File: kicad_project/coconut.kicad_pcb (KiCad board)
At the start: 2 copper layers, 212.6 x 79.2 mm, 88 parts

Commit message: change the layout
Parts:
- K_32: footprint MX_Only:MXOnly-1U-NoLED -> MX_Only:MXOnly-1.25U-NoLED
- K_34: footprint MX_Only:MXOnly-1.5U-NoLED -> MX_Only:MXOnly-1.25U-NoLED
- moved K_33 4.76 mm to (58.7, 68.2)
- moved REF** 3.57 mm to (69.4, 76.0)
- moved K_34 2.38 mm to (80.1, 68.2)
- moved K_32 2.38 mm to (37.2, 68.2)
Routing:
- net col2: track 207.8 -> 209.8 mm
- net col1: track 228.7 -> 229.6 mm

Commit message: fix mismatch
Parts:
- moved D_32 4.76 mm to (48.1, 68.9)
- moved D_33 4.76 mm to (67.2, 68.9)
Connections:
- U_1 pad 10: col3 -> col2
- U_1 pad 7: col0 -> col3
- U_1 pad 8: col1 -> col0
- U_1 pad 9: col2 -> col1
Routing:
- net col3: track 187.8 -> 197.6 mm
- net col2: track 209.8 -> 206.8 mm
- net col1: track 229.6 -> 226.7 mm
- net col0: track 243.3 -> 240.3 mm
- net Net-(D_32-Pad2): track 7.70 -> 10.1 mm
- net Net-(D_34-Pad2): track 12.5 -> 10.1 mm
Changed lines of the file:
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@@
       (net 14 "row2") (pinfunction "D0") (pintype "bidirectional"))
     (pad "7" thru_hole oval locked (at 15.24 12.7 90) (size 1.6 1.6) (drill 0.8) (layers *.Cu *.Mask)
-      (net 1 "col0") (pinfunction "D4") (pintype "bidirectional"))
+      (net 4 "col3") (pinfunction "D4") (pintype "bidirectional"))
     (pad "8" thru_hole oval locked (at 15.24 10.16 90) (size 1.6 1.6) (drill 0.8) (layers *.Cu *.Mask)
-      (net 2 "col1") (pinfunction "C6") (pintype "bidirectional"))
+      (net 1 "col0") (pinfunction "C6") (pintype "bidirectional"))
     (pad "9" thru_hole oval locked (at 15.24 7.62 90) (size 1.6 1.6) (drill 0.8) (layers *.Cu *.Mask)
-      (net 3 "col2") (pinfunction "D7") (pintype "bidirectional"))
+      (net 2 "col1") (pinfunction "D7") (pintype "bidirectional"))
     (pad "10" thru_hole oval locked (at 15.24 5.08 90) (size 1.6 1.6) (drill 0.8) (layers *.Cu *.Mask)
-      (net 4 "col3") (pinfunction "E6") (pintype "bidirectional"))
+      (net 3 "col2") (pinfunction "E6") (pintype "bidirectional"))
     (pad "11" thru_hole oval locked (at 15.24 2.54 90) (size 1.6 1.6) (drill 0.8) (layers *.Cu *.Mask)
       (net 10 "col9") (pinfunction "B4") (pintype "bidirectional"))
@@
   )
   (footprint "Diode_SMD:D_SOD-123" (layer "B.Cu")
-    (at 43.3625 68.893901 90)
+    (at 48.1265 68.893901 90)
     (descr "SOD-123")
     (tags "SOD-123")
@@
   )
   (footprint "Diode_SMD:D_SOD-123" (layer "B.Cu")
-    (at 62.4125 68.893901 90)
+    (at 67.1765 68.893901 90)
     (descr "SOD-123")
     (tags "SOD-123")
@@
   (segment (start 11.9775 27.535) (end 11.9775 41.8225) (width 0.25) (layer "F.Cu") (net 1))
   (segment (start 7.215 8.485) (end 7.215 22.7725) (width 0.25) (layer "F.Cu") (net 1))
-  (via (at 16.74 52.493901) (size 0.8) (drill 0.4) (layers "F.Cu" "B.Cu") (net 1))
-  (segment (start 184.573901 52.493901) (end 192.635 60.555) (width 0.25) (layer "B.Cu") (net 1))
-  (segment (start 16.74 52.493901) (end 184.573901 52.493901) (width 0.25) (layer "B.Cu") (net 1))
+  (via (at 16.74 53.493901) (size 0.8) (drill 0.4) (layers "F.Cu" "B.Cu") (net 1))
+  (segment (start 183.033901 53.493901) (end 16.74 53.493901) (width 0.25) (layer "B.Cu") (net 1))
+  (segment (start 190.095 60.555) (end 183.033901 53.493901) (width 0.25) (layer "B.Cu") (net 1))
   (segment (start 33.4085 65.635) (end 26.9 59.1265) (width 0.25) (layer "F.Cu") (net 2))
   (segment (start 31.0275 40.8545) (end 26.9 44.982) (width 0.25) (layer "F.Cu") (net 2))
@@
   (segment (start 26.265 22.7725) (end 31.0275 27.535) (width 0.25) (layer "F.Cu") (net 2))
   (segment (start 26.265 8.485) (end 26.265 22.7725) (width 0.25) (layer "F.Cu") (net 2))
-  (via (at 26.9 53.493901) (size 0.8) (drill 0.4) (layers "F.Cu" "B.Cu") (net 2))
-  (segment (start 190.095 60.555) (end 183.033901 53.493901) (width 0.25) (layer "B.Cu") (net 2))
-  (segment (start 183.033901 53.493901) (end 26.9 53.493901) (width 0.25) (layer "B.Cu") (net 2))
+  (via (at 26.9 54.493901) (size 0.8) (drill 0.4) (layers "F.Cu" "B.Cu") (net 2))
+  (segment (start 26.9 54.493901) (end 181.493901 54.493901) (width 0.25) (layer "B.Cu") (net 2))
+  (segment (start 181.493901 54.493901) (end 187.555 60.555) (width 0.25) (layer "B.Cu") (net 2))
   (segment (start 50.0775 41.8225) (end 45.315 46.585) (width 0.25) (layer "F.Cu") (net 3))
   (segment (start 54.8405 65.635) (end 45.315 56.1095) (width 0.25) (layer "F.Cu") (net 3))
@@
   (segment (start 45.315 22.7725) (end 50.0775 27.535) (width 0.25) (layer "F.Cu") (net 3))
   (segment (start 45.315 8.485) (end 45.315 22.7725) (width 0.25) (layer "F.Cu") (net 3))
-  (via (at 45.315 54.493901) (size 0.8) (drill 0.4) (layers "F.Cu" "B.Cu") (net 3))
-  (segment (start 181.493901 54.493901) (end 187.555 60.555) (width 0.25) (layer "B.Cu") (net 3))
-  (segment (start 45.315 54.493901) (end 181.493901 54.493901) (width 0.25) (layer "B.Cu") (net 3))
+  (via (at 45.315 55.493901) (size 0.8) (drill 0.4) (layers "F.Cu" "B.Cu") (net 3))
+  (segment (start 179.953901 55.493901) (end 45.315 55.493901) (width 0.25) (layer "B.Cu") (net 3))
+  (segment (start 179.953901 55.493901) (end 185.015 60.555) (width 0.25) (layer "B.Cu") (net 3))
   (segment (start 69.1275 27.535) (end 69.1275 41.8225) (width 0.25) (layer "F.Cu") (net 4))
+  (segment (start 64.365 46.585) (end 64.365 53.728) (width 0.25) (layer "F.Cu") (net 4))
   (segment (start 64.365 8.485) (end 64.365 22.7725) (width 0.25) (layer "F.Cu") (net 4))
   (segment (start 69.1275 41.8225) (end 64.365 46.585) (width 0.25) (layer "F.Cu") (net 4))
-  (segment (start 64.365 56.11) (end 73.89 65.635) (width 0.25) (layer "F.Cu") (net 4))
-  (segment (start 64.365 46.585) (end 64.365 55.523) (width 0.25) (layer "F.Cu") (net 4))
-  (segment (start 64.365 55.523) (end 64.365 56.11) (width 0.25) (layer "F.Cu") (net 4))
+  (segment (start 76.272 65.635) (end 64.365 53.728) (width 0.25) (layer "F.Cu") (net 4))
   (segment (start 64.365 22.7725) (end 69.1275 27.535) (width 0.25) (layer "F.Cu") (net 4))
-  (via (at 64.365 55.493901) (size 0.8) (drill 0.4) (layers "F.Cu" "B.Cu") (net 4))
-  (segment (start 64.365 55.493901) (end 179.953901 55.493901) (width 0.25) (layer "B.Cu") (net 4))
-  (segment (start 179.953901 55.493901) (end 185.015 60.555) (width 0.25) (layer "B.Cu") (net 4))
-  (segment (start 83.415 46.585) (end 83.415 56.493901) (width 0.25) (layer "F.Cu") (net 5))
+  (via (at 64.365 52.493901) (size 0.8) (drill 0.4) (layers "F.Cu" "B.Cu") (net 4))
+  (segment (start 184.573901 52.493901) (end 192.635 60.555) (width 0.25) (layer "B.Cu") (net 4))
+  (segment (start 64.365 52.493901) (end 184.573901 52.493901) (width 0.25) (layer "B.Cu") (net 4))
   (segment (start 88.1775 27.535) (end 88.1775 41.8225) (width 0.25) (layer "F.Cu") (net 5))
   (segment (start 83.415 8.485) (end 83.415 22.7725) (width 0.25) (layer "F.Cu") (net 5))
+  (segment (start 83.415 46.585) (end 83.415 56.493901) (width 0.25) (layer "F.Cu") (net 5))
   (segment (start 83.415 22.7725) (end 88.1775 27.535) (width 0.25) (layer "F.Cu") (net 5))
   (segment (start 88.1775 41.8225) (end 83.415 46.585) (width 0.25) (layer "F.Cu") (net 5))
@@
   (segment (start 20.163599 63.095) (end 24.3125 67.243901) (width 0.25) (layer "B.Cu") (net 47))
   (segment (start 15.94625 63.095) (end 20.163599 63.095) (width 0.25) (layer "B.Cu") (net 47))
-  (segment (start 37.3775 63.095) (end 39.213599 63.095) (width 0.25) (layer "B.Cu") (net 48))
-  (segment (start 39.213599 63.095) (end 43.3625 67.243901) (width 0.25) (layer "B.Cu") (net 48))
-  (segment (start 58.263599 63.095) (end 62.4125 67.243901) (width 0.25) (layer "B.Cu") (net 49))
-  (segment (start 56.4275 63.095) (end 58.263599 63.095) (width 0.25) (layer "B.Cu") (net 49))
+  (segment (start 39.7585 63.095) (end 43.977599 63.095) (width 0.25) (layer "B.Cu") (net 48))
+  (segment (start 43.977599 63.095) (end 48.1265 67.243901) (width 0.25) (layer "B.Cu") (net 48))
+  (segment (start 61.1905 63.095) (end 63.027599 63.095) (width 0.25) (layer "B.Cu") (net 49))
+  (segment (start 63.027599 63.095) (end 67.1765 67.243901) (width 0.25) (layer "B.Cu") (net 49))
   (segment (start 86.838599 63.095) (end 90.9875 67.243901) (width 0.25) (layer "B.Cu") (net 50))
-  (segment (start 80.24 63.095) (end 86.838599 63.095) (width 0.25) (layer "B.Cu") (net 50))
+  (segment (start 82.622 63.095) (end 86.838599 63.095) (width 0.25) (layer "B.Cu") (net 50))
   (segment (start 115.95875 63.095) (end 129.701099 63.095) (width 0.25) (layer "B.Cu") (net 51))
   (segment (start 129.701099 63.095) (end 133.85 67.243901) (width 0.25) (layer "B.Cu") (net 51))

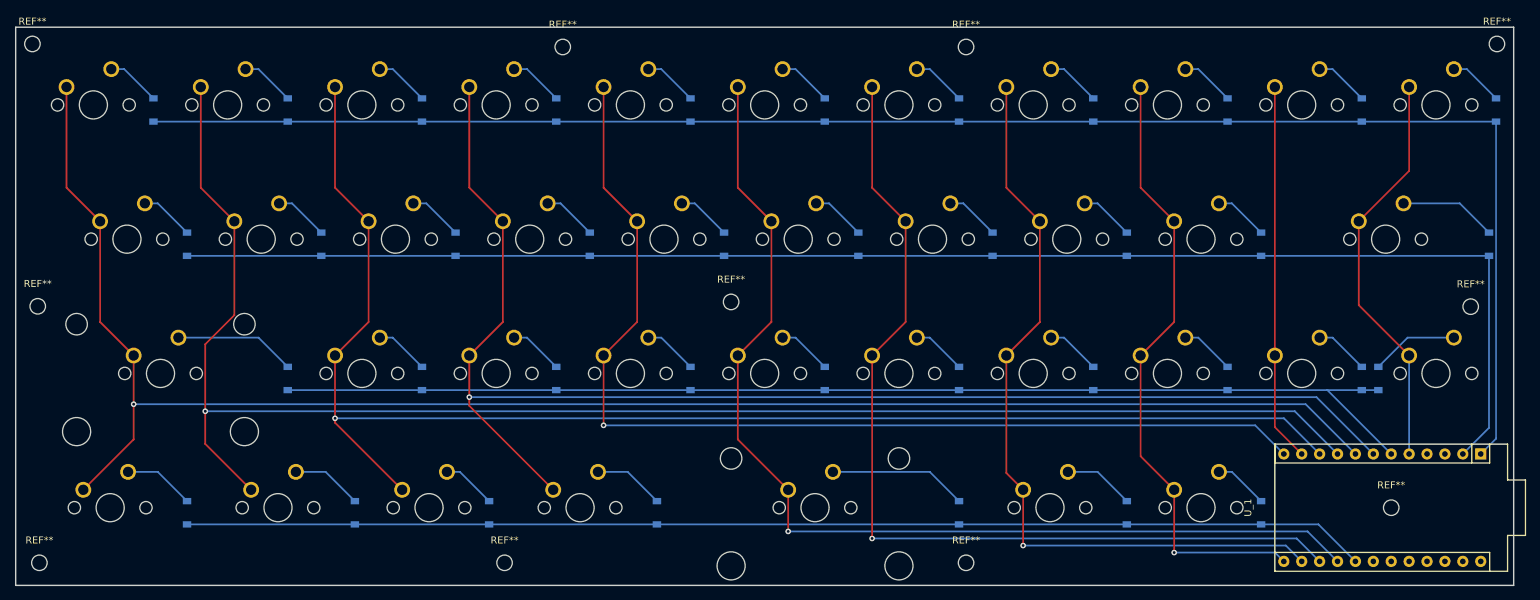
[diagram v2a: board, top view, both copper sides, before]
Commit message: add clearance
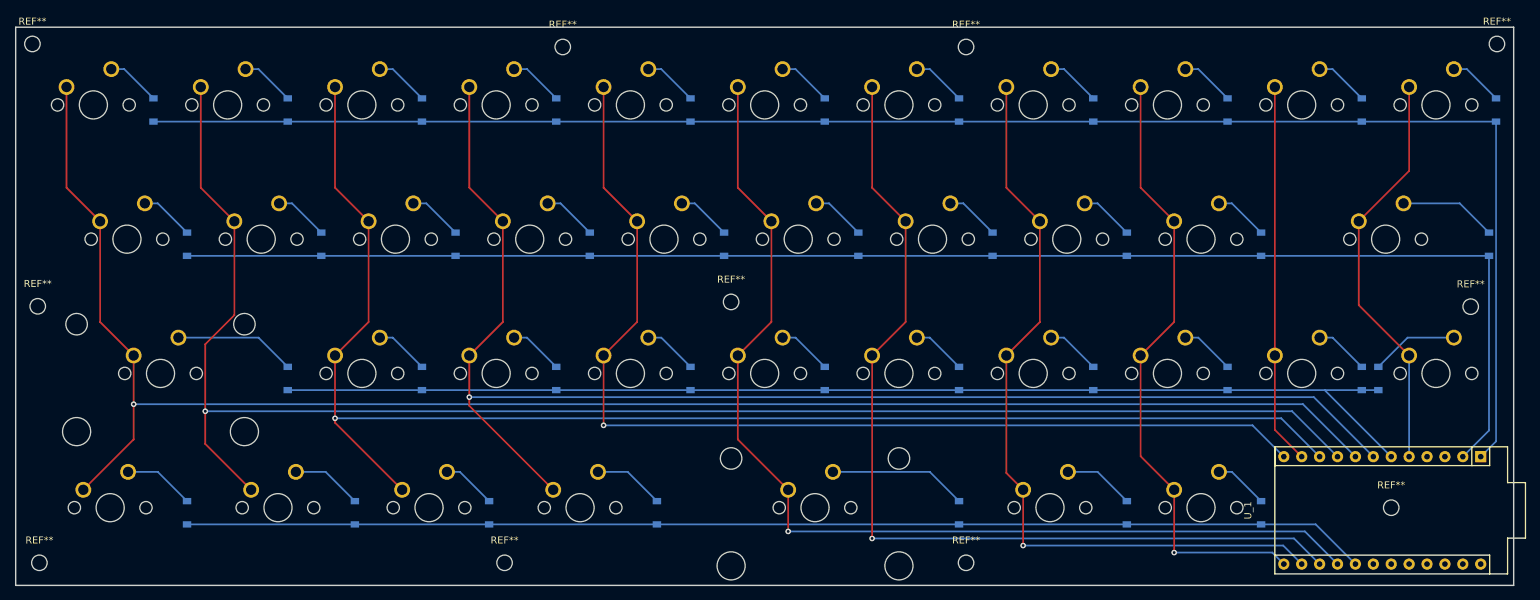
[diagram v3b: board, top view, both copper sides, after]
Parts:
- moved U_1 0.38 mm to (179.9, 76.2)
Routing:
- net row2: track 167.6 -> 168.1 mm
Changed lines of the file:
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@@
   )
   (footprint "Arduino:Sparkfun_Pro_Micro" (layer "F.Cu")
-    (at 179.935 75.795 90)
+    (at 179.935 76.176 90)
     (descr "Sparkfun Pro Micro")
     (tags "Arduino Sparkfun Pro Micro")
@@
   (segment (start 7.215 8.485) (end 7.215 22.7725) (width 0.25) (layer "F.Cu") (net 1))
   (via (at 16.74 53.493901) (size 0.8) (drill 0.4) (layers "F.Cu" "B.Cu") (net 1))
-  (segment (start 183.033901 53.493901) (end 16.74 53.493901) (width 0.25) (layer "B.Cu") (net 1))
-  (segment (start 190.095 60.555) (end 183.033901 53.493901) (width 0.25) (layer "B.Cu") (net 1))
+  (segment (start 190.095 60.936) (end 182.652901 53.493901) (width 0.25) (layer "B.Cu") (net 1))
+  (segment (start 16.74 53.493901) (end 182.652901 53.493901) (width 0.25) (layer "B.Cu") (net 1))
   (segment (start 33.4085 65.635) (end 26.9 59.1265) (width 0.25) (layer "F.Cu") (net 2))
   (segment (start 31.0275 40.8545) (end 26.9 44.982) (width 0.25) (layer "F.Cu") (net 2))
@@
   (segment (start 26.265 8.485) (end 26.265 22.7725) (width 0.25) (layer "F.Cu") (net 2))
   (via (at 26.9 54.493901) (size 0.8) (drill 0.4) (layers "F.Cu" "B.Cu") (net 2))
-  (segment (start 26.9 54.493901) (end 181.493901 54.493901) (width 0.25) (layer "B.Cu") (net 2))
-  (segment (start 181.493901 54.493901) (end 187.555 60.555) (width 0.25) (layer "B.Cu") (net 2))
+  (segment (start 181.112901 54.493901) (end 26.9 54.493901) (width 0.25) (layer "B.Cu") (net 2))
+  (segment (start 187.555 60.936) (end 181.112901 54.493901) (width 0.25) (layer "B.Cu") (net 2))
   (segment (start 50.0775 41.8225) (end 45.315 46.585) (width 0.25) (layer "F.Cu") (net 3))
   (segment (start 54.8405 65.635) (end 45.315 56.1095) (width 0.25) (layer "F.Cu") (net 3))
@@
   (segment (start 45.315 8.485) (end 45.315 22.7725) (width 0.25) (layer "F.Cu") (net 3))
   (via (at 45.315 55.493901) (size 0.8) (drill 0.4) (layers "F.Cu" "B.Cu") (net 3))
-  (segment (start 179.953901 55.493901) (end 45.315 55.493901) (width 0.25) (layer "B.Cu") (net 3))
-  (segment (start 179.953901 55.493901) (end 185.015 60.555) (width 0.25) (layer "B.Cu") (net 3))
+  (segment (start 45.315 55.493901) (end 179.572901 55.493901) (width 0.25) (layer "B.Cu") (net 3))
+  (segment (start 185.015 60.936) (end 179.572901 55.493901) (width 0.25) (layer "B.Cu") (net 3))
   (segment (start 69.1275 27.535) (end 69.1275 41.8225) (width 0.25) (layer "F.Cu") (net 4))
   (segment (start 64.365 46.585) (end 64.365 53.728) (width 0.25) (layer "F.Cu") (net 4))
@@
   (segment (start 64.365 22.7725) (end 69.1275 27.535) (width 0.25) (layer "F.Cu") (net 4))
   (via (at 64.365 52.493901) (size 0.8) (drill 0.4) (layers "F.Cu" "B.Cu") (net 4))
-  (segment (start 184.573901 52.493901) (end 192.635 60.555) (width 0.25) (layer "B.Cu") (net 4))
-  (segment (start 64.365 52.493901) (end 184.573901 52.493901) (width 0.25) (layer "B.Cu") (net 4))
+  (segment (start 184.192901 52.493901) (end 64.365 52.493901) (width 0.25) (layer "B.Cu") (net 4))
+  (segment (start 192.635 60.936) (end 184.192901 52.493901) (width 0.25) (layer "B.Cu") (net 4))
   (segment (start 88.1775 27.535) (end 88.1775 41.8225) (width 0.25) (layer "F.Cu") (net 5))
   (segment (start 83.415 8.485) (end 83.415 22.7725) (width 0.25) (layer "F.Cu") (net 5))
@@
   (segment (start 88.1775 41.8225) (end 83.415 46.585) (width 0.25) (layer "F.Cu") (net 5))
   (via (at 83.415 56.493901) (size 0.8) (drill 0.4) (layers "F.Cu" "B.Cu") (net 5))
-  (segment (start 83.415 56.493901) (end 175.873901 56.493901) (width 0.25) (layer "B.Cu") (net 5))
-  (segment (start 175.873901 56.493901) (end 179.935 60.555) (width 0.25) (layer "B.Cu") (net 5))
+  (segment (start 175.492901 56.493901) (end 83.415 56.493901) (width 0.25) (layer "B.Cu") (net 5))
+  (segment (start 179.935 60.936) (end 175.492901 56.493901) (width 0.25) (layer "B.Cu") (net 5))
   (segment (start 109.60875 65.635) (end 109.60875 71.543901) (width 0.25) (layer "F.Cu") (net 6))
   (segment (start 109.60875 65.635) (end 102.465 58.49125) (width 0.25) (layer "F.Cu") (net 6))
@@
   (segment (start 102.465 46.585) (end 102.465 58.49125) (width 0.25) (layer "F.Cu") (net 6))
   (via (at 109.60875 71.543901) (size 0.8) (drill 0.4) (layers "F.Cu" "B.Cu") (net 6))
-  (segment (start 109.60875 71.543901) (end 183.303901 71.543901) (width 0.25) (layer "B.Cu") (net 6))
-  (segment (start 183.303901 71.543901) (end 187.555 75.795) (width 0.25) (layer "B.Cu") (net 6))
+  (segment (start 182.922901 71.543901) (end 109.60875 71.543901) (width 0.25) (layer "B.Cu") (net 6))
+  (segment (start 187.555 76.176) (end 182.922901 71.543901) (width 0.25) (layer "B.Cu") (net 6))
   (segment (start 121.515 46.585) (end 121.515 72.541) (width 0.25) (layer "F.Cu") (net 7))
   (segment (start 121.515 72.541) (end 121.515 72.543901) (width 0.25) (layer "F.Cu") (net 7))
@@
   (segment (start 126.2775 27.535) (end 126.2775 41.8225) (width 0.25) (layer "F.Cu") (net 7))
   (via (at 121.515 72.541) (size 0.8) (drill 0.4) (layers "F.Cu" "B.Cu") (net 7))
-  (segment (start 181.761 72.541) (end 185.015 75.795) (width 0.25) (layer "B.Cu") (net 7))
-  (segment (start 121.515 72.541) (end 181.761 72.541) (width 0.25) (layer "B.Cu") (net 7))
+  (segment (start 181.38 72.541) (end 185.015 76.176) (width 0.25) (layer "B.Cu") (net 7))
+  (segment (start 121.515 72.541) (end 181.38 72.541) (width 0.25) (layer "B.Cu") (net 7))
   (segment (start 140.565 22.7725) (end 145.3275 27.535) (width 0.25) (layer "F.Cu") (net 8))
   (segment (start 140.565 8.485) (end 140.565 22.7725) (width 0.25) (layer "F.Cu") (net 8))
@@
   (segment (start 145.3275 41.8225) (end 140.565 46.585) (width 0.25) (layer "F.Cu") (net 8))
   (via (at 142.94625 73.543901) (size 0.8) (drill 0.4) (layers "F.Cu" "B.Cu") (net 8))
-  (segment (start 180.223901 73.543901) (end 182.475 75.795) (width 0.25) (layer "B.Cu") (net 8))
-  (segment (start 142.94625 73.543901) (end 180.223901 73.543901) (width 0.25) (layer "B.Cu") (net 8))
+  (segment (start 179.842901 73.543901) (end 142.94625 73.543901) (width 0.25) (layer "B.Cu") (net 8))
+  (segment (start 179.842901 73.543901) (end 182.475 76.176) (width 0.25) (layer "B.Cu") (net 8))
   (segment (start 164.3775 27.535) (end 164.3775 41.8225) (width 0.25) (layer "F.Cu") (net 9))
   (segment (start 159.615 46.585) (end 159.615 60.8725) (width 0.25) (layer "F.Cu") (net 9))
@@
   (segment (start 159.615 60.8725) (end 164.3775 65.635) (width 0.25) (layer "F.Cu") (net 9))
   (via (at 164.3775 74.543901) (size 0.8) (drill 0.4) (layers "F.Cu" "B.Cu") (net 9))
-  (segment (start 179.935 75.795) (end 178.683901 74.543901) (width 0.25) (layer "B.Cu") (net 9))
-  (segment (start 178.683901 74.543901) (end 164.3775 74.543901) (width 0.25) (layer "B.Cu") (net 9))
+  (segment (start 164.3775 74.543901) (end 178.302901 74.543901) (width 0.25) (layer "B.Cu") (net 9))
+  (segment (start 179.935 76.176) (end 178.302901 74.543901) (width 0.25) (layer "B.Cu") (net 9))
   (segment (start 178.665 8.485) (end 178.665 46.585) (width 0.25) (layer "F.Cu") (net 10))
-  (segment (start 178.665 46.585) (end 178.665 56.745) (width 0.25) (layer "F.Cu") (net 10))
-  (segment (start 178.665 56.745) (end 182.475 60.555) (width 0.25) (layer "F.Cu") (net 10))
+  (segment (start 182.475 60.936) (end 178.665 57.126) (width 0.25) (layer "F.Cu") (net 10))
+  (segment (start 178.665 57.126) (end 178.665 46.585) (width 0.25) (layer "F.Cu") (net 10))
   (segment (start 190.57125 39.44125) (end 197.715 46.585) (width 0.25) (layer "F.Cu") (net 11))
   (segment (start 190.57125 27.535) (end 190.57125 39.44125) (width 0.25) (layer "F.Cu") (net 11))
   (segment (start 197.715 8.485) (end 197.715 20.39125) (width 0.25) (layer "F.Cu") (net 11))
   (segment (start 197.715 20.39125) (end 190.57125 27.535) (width 0.25) (layer "F.Cu") (net 11))
-  (segment (start 197.715 46.585) (end 197.715 60.555) (width 0.25) (layer "B.Cu") (net 11))
-  (segment (start 210.05 58.38) (end 207.875 60.555) (width 0.25) (layer "B.Cu") (net 12))
+  (segment (start 197.715 60.936) (end 197.715 46.585) (width 0.25) (layer "B.Cu") (net 11))
   (segment (start 210.05 13.393901) (end 19.55 13.393901) (width 0.25) (layer "B.Cu") (net 12))
-  (segment (start 210.05 13.393901) (end 210.05 58.38) (width 0.25) (layer "B.Cu") (net 12))
-  (segment (start 209.05 56.84) (end 205.335 60.555) (width 0.25) (layer "B.Cu") (net 13))
+  (segment (start 207.875 60.936) (end 210.05 58.761) (width 0.25) (layer "B.Cu") (net 12))
+  (segment (start 210.05 58.761) (end 210.05 13.393901) (width 0.25) (layer "B.Cu") (net 12))
+  (segment (start 205.335 60.936) (end 209.05 57.221) (width 0.25) (layer "B.Cu") (net 13))
+  (segment (start 209.05 57.221) (end 209.05 32.443901) (width 0.25) (layer "B.Cu") (net 13))
   (segment (start 209.05 32.443901) (end 24.3125 32.443901) (width 0.25) (layer "B.Cu") (net 13))
-  (segment (start 209.05 32.443901) (end 209.05 56.84) (width 0.25) (layer "B.Cu") (net 13))
-  (segment (start 195.175 60.555) (end 186.113901 51.493901) (width 0.25) (layer "B.Cu") (net 14))
   (segment (start 193.35 51.493901) (end 38.6 51.493901) (width 0.25) (layer "B.Cu") (net 14))
-  (segment (start 184.843901 70.543901) (end 190.095 75.795) (width 0.25) (layer "B.Cu") (net 15))
-  (segment (start 184.843901 70.543901) (end 24.3125 70.543901) (width 0.25) (layer "B.Cu") (net 15))
+  (segment (start 195.175 60.936) (end 185.732901 51.493901) (width 0.25) (layer "B.Cu") (net 14))
+  (segment (start 190.095 76.176) (end 184.462901 70.543901) (width 0.25) (layer "B.Cu") (net 15))
+  (segment (start 184.462901 70.543901) (end 24.3125 70.543901) (width 0.25) (layer "B.Cu") (net 15))
   (segment (start 13.565 5.945) (end 15.401099 5.945) (width 0.25) (layer "B.Cu") (net 16))
   (segment (start 15.401099 5.945) (end 19.55 10.093901) (width 0.25) (layer "B.Cu") (net 16))

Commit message: fix holes
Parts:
- moved REF** 0.37 mm to (195.2, 68.5)
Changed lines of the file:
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@@
   )
   (footprint "MountingHole:MountingHole_2.2mm_M2" (layer "F.Cu")
-    (at 195.175 68.177)
+    (at 195.175 68.55)
     (descr "Mounting Hole 2.2mm, no annular, M2")
     (tags "mounting hole 2.2mm no annular m2")
